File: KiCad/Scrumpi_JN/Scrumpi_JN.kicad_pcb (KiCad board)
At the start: 4 copper layers, 165.1 x 127 mm, 203 parts

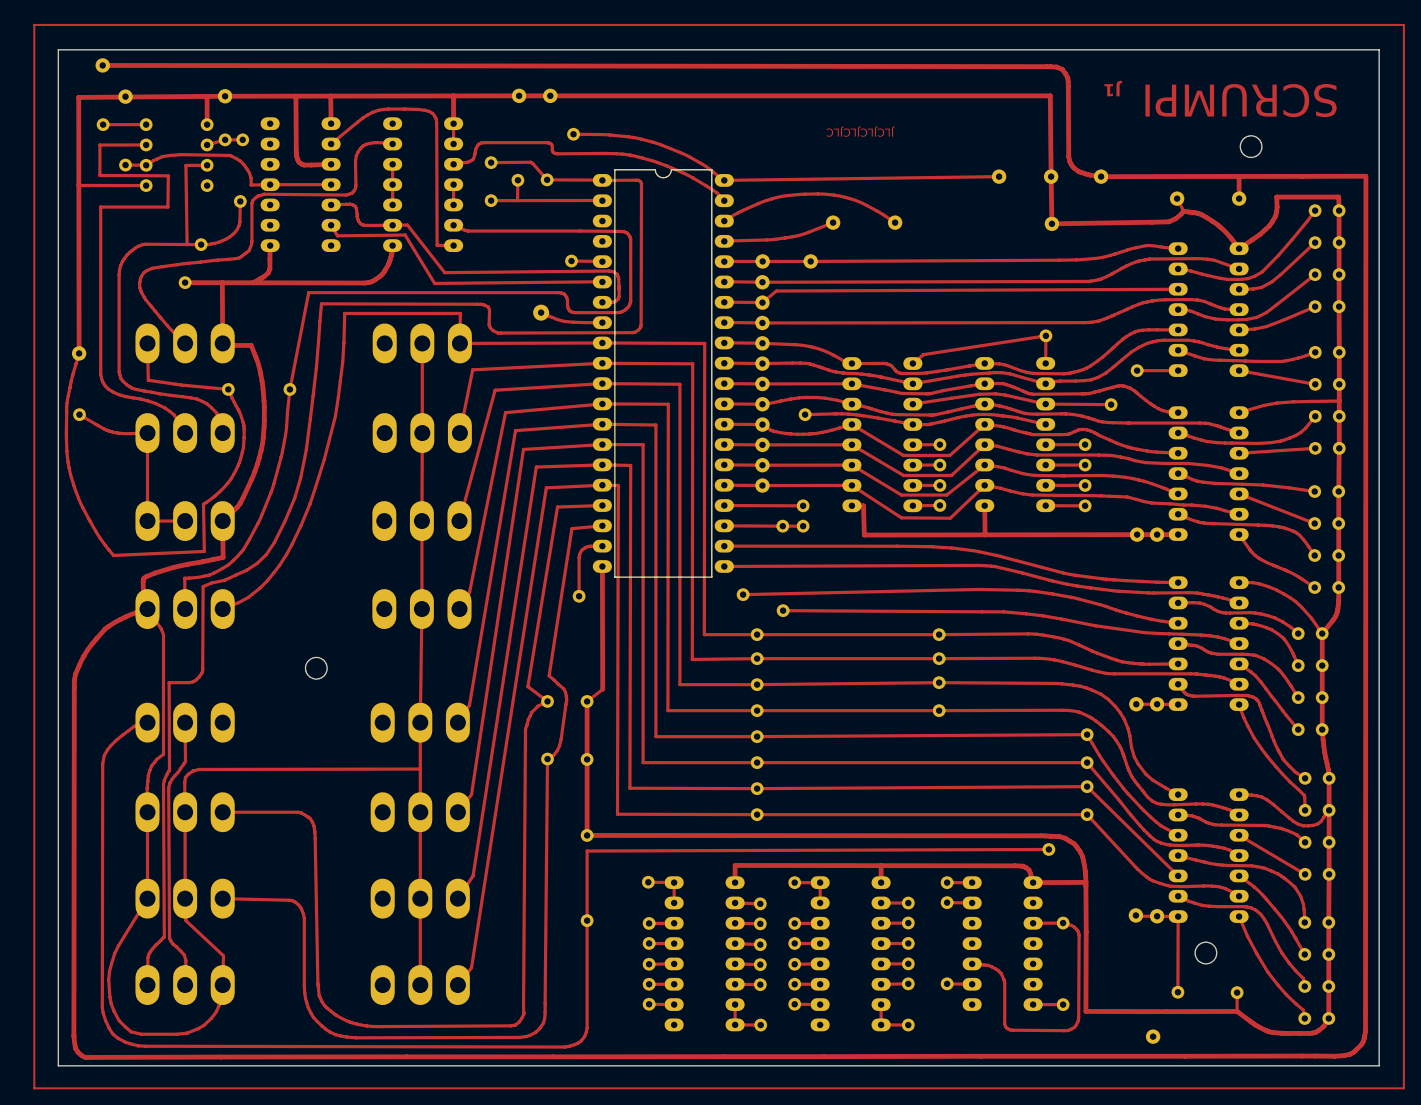
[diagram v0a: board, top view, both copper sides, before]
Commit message: Updated Silk Screen
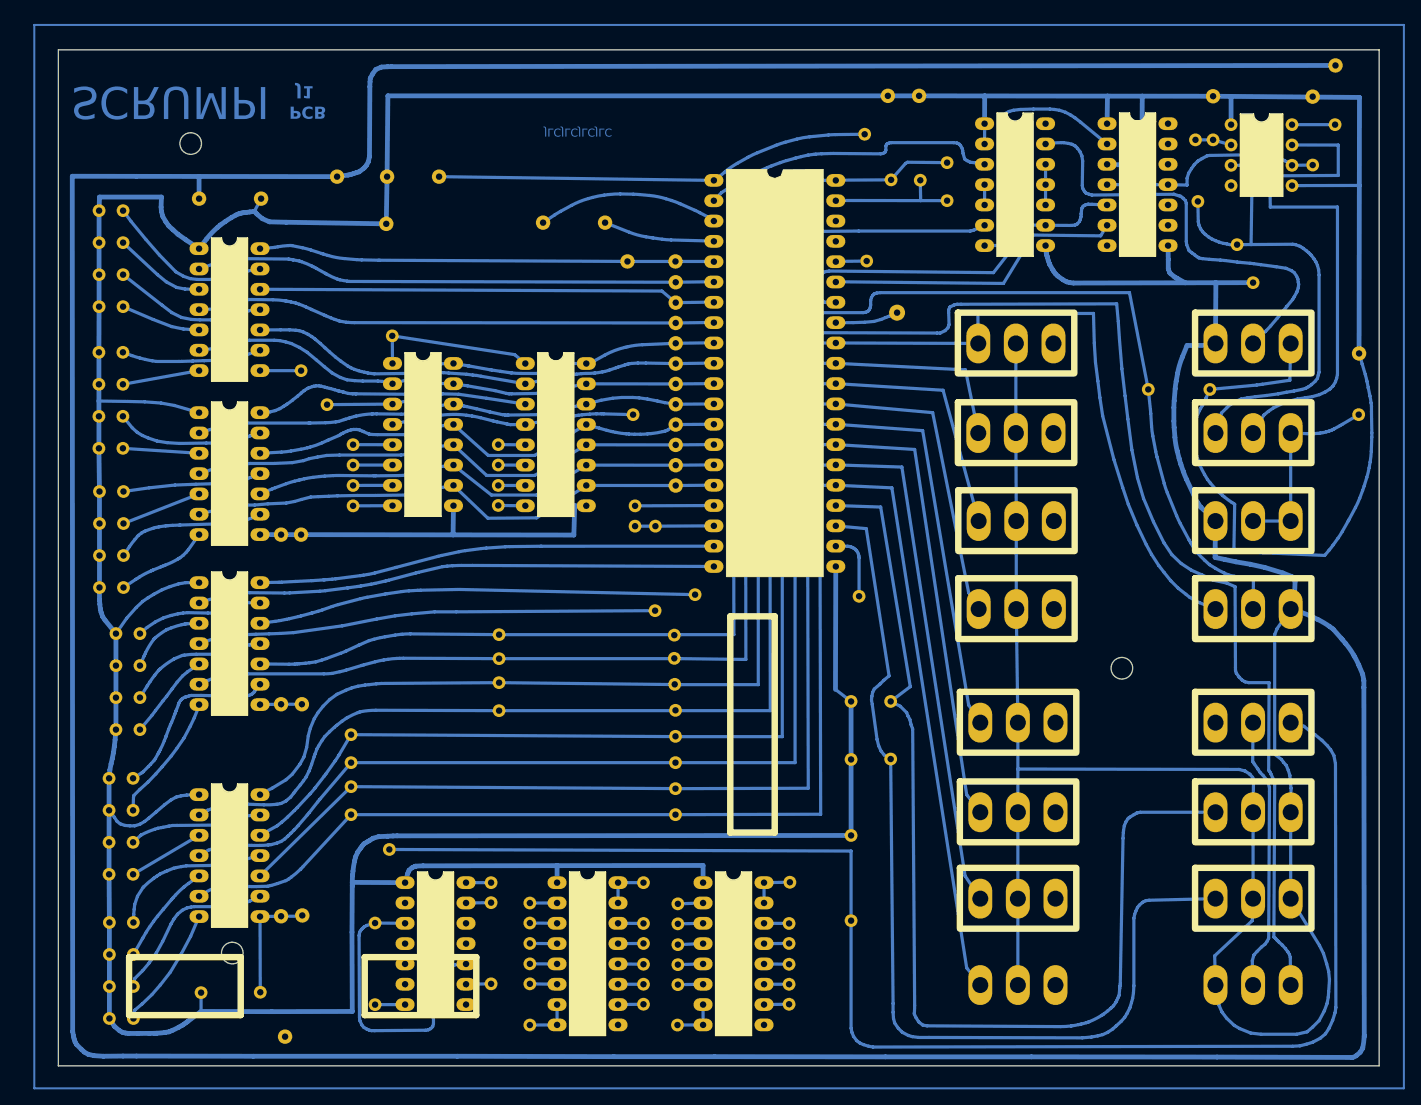
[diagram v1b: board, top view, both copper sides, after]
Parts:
- ? (x171), REF** (x31): moved to F.Cu
- REF**: moved to B.Cu
- moved ? 160.0 mm to (239.3, 64.4), turned to 0 degrees
- moved ? 159.9 mm to (239.2, 72.0), turned to 0 degrees
- moved ? 155.0 mm to (81.8, 76.2), turned to 0 degrees
- moved ? 155.0 mm to (81.8, 68.2), turned to 0 degrees
- moved ? 155.0 mm to (81.8, 64.2), turned to 0 degrees
- moved ? 155.0 mm to (81.8, 72.2), turned to 0 degrees
- moved ? 155.0 mm to (81.8, 50.5), turned to 0 degrees
- moved ? 155.0 mm to (81.8, 46.5), turned to 0 degrees
- moved ? 155.0 mm to (81.8, 58.5), turned to 0 degrees
- moved ? 155.0 mm to (81.8, 54.5), turned to 0 degrees
- moved ? 154.9 mm to (81.8, 85.6), turned to 0 degrees
- moved ? 154.9 mm to (81.8, 93.6), turned to 0 degrees
- moved ? 154.9 mm to (81.8, 89.6), turned to 0 degrees
- moved ? 154.9 mm to (81.8, 81.6), turned to 0 degrees
- moved ? 154.1 mm to (236.3, 28.4), turned to 0 degrees
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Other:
- board text added: "PCB"
- board text added: "PCB-J1"

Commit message: Updated Silk Screen
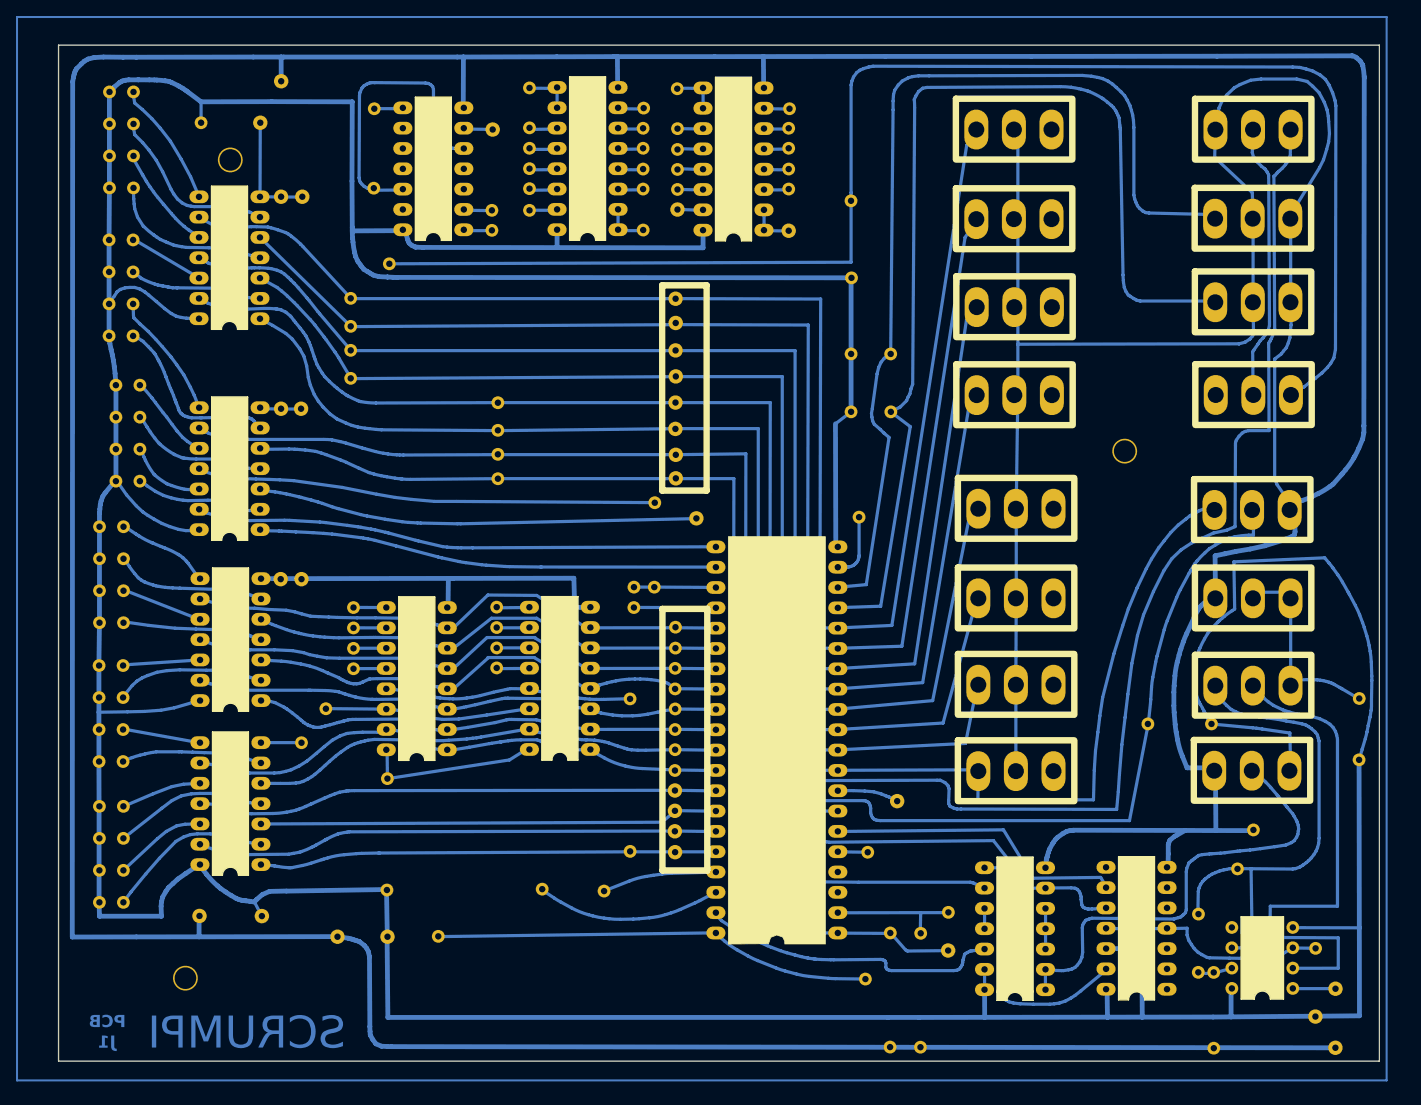
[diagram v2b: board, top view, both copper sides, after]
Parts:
- moved ? 131.5 mm to (236.3, 151.2)
- moved ? 131.4 mm to (102.2, 134.7)
- moved ? 117.4 mm to (116.1, 43.7)
- moved ? 117.1 mm to (135.6, 31.2)
- moved ? 115.8 mm to (233.8, 147.3)
- moved ? 113.7 mm to (117.8, 117.5)
- moved REF** 110.6 mm to (215.3, 143.9), turned to 180 degrees
- moved ? 110.4 mm to (116.2, 33.8)
- moved ? 108.7 mm to (94.5, 35.5)
- moved REF** 108.5 mm to (200.1, 143.9), turned to 180 degrees
- moved REF** 108.2 mm to (231.0, 143.8), turned to 180 degrees
- moved ? 107.0 mm to (181.6, 120.3)
- moved ? 106.2 mm to (219.2, 141.8)
- moved ? 101.9 mm to (154.1, 31.3)
- moved ? 100.6 mm to (144.9, 131.6)
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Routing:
- net (no net): track 5815.1 -> 5836.7 mm
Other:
- board text removed: "JLCJLCJLCJLC"

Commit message: Updated Silk Screen
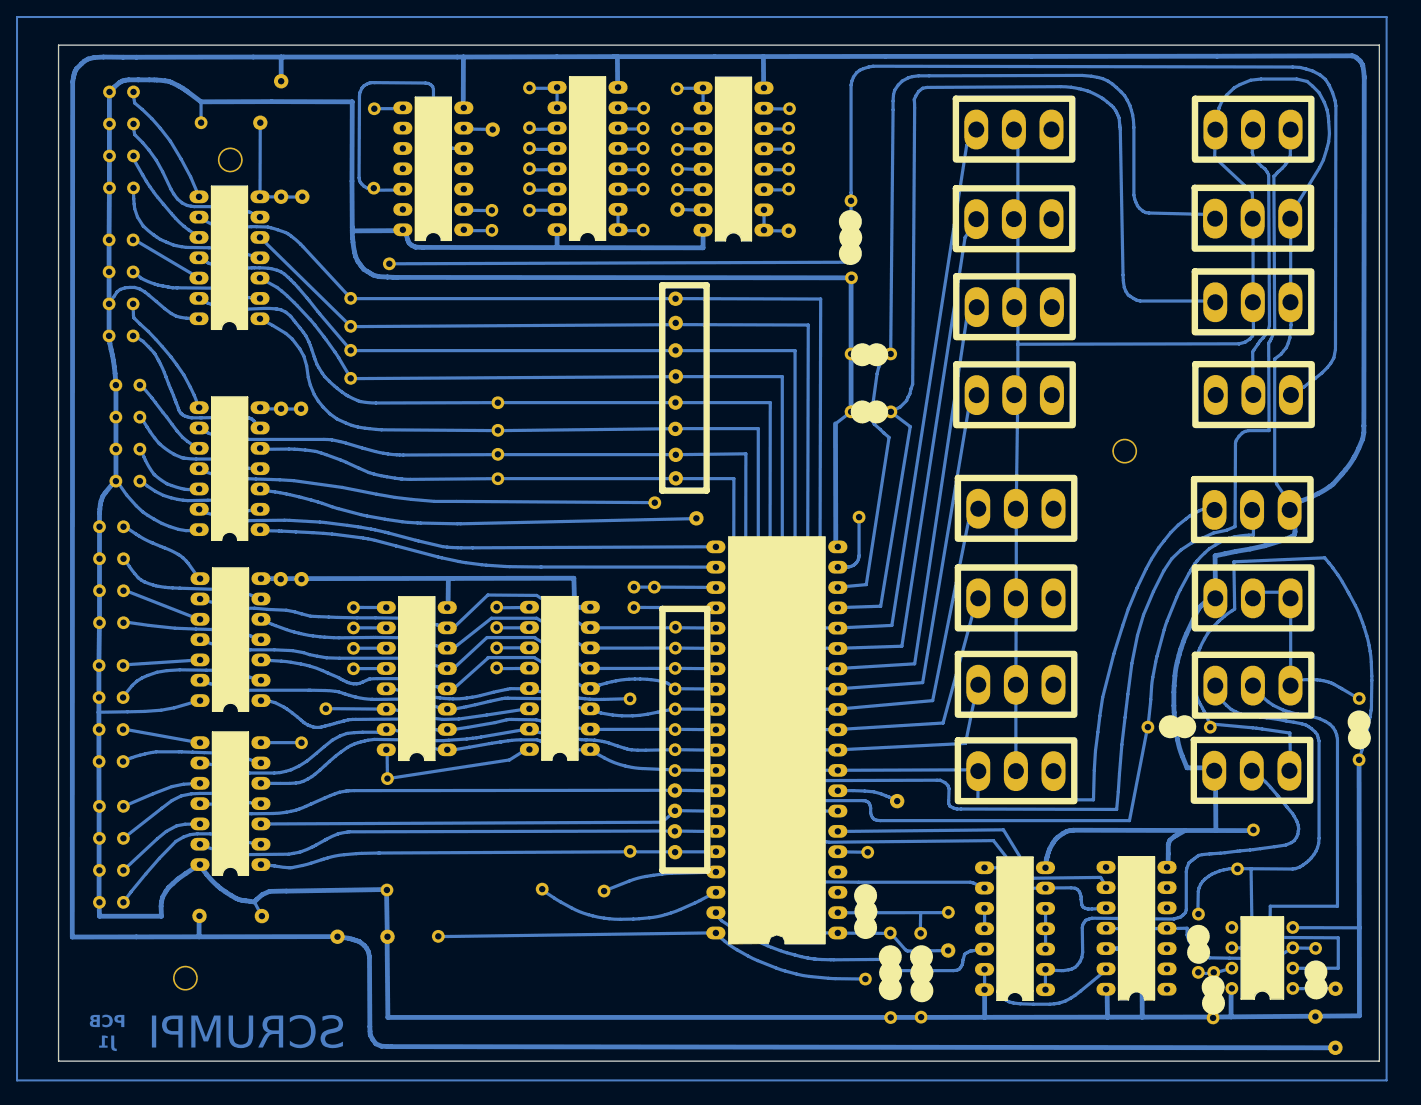
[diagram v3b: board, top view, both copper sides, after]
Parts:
- moved ? 3.78 mm to (221.1, 147.4)
- moved ? 3.76 mm to (184.6, 147.3)
- moved ? 3.69 mm to (180.8, 147.4)
- moved ? 0.43 mm to (220.7, 111.1)
- moved ? 0.40 mm to (212.9, 111.1)
